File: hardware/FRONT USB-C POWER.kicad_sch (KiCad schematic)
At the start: 40 parts, among them Q3 PMPB11EN,115, Q4 PMPB11EN,115, Q5 PMPB11EN,115, Q6 PMPB11EN,115, U7 LM5143

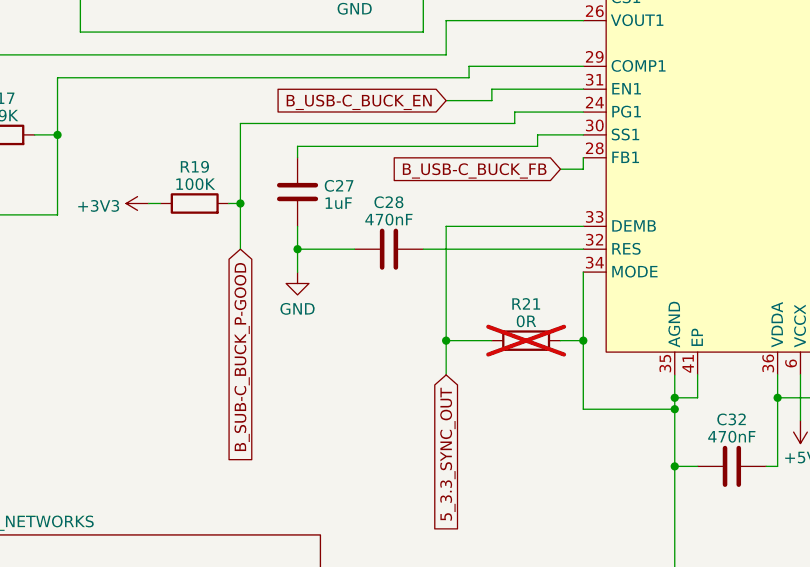
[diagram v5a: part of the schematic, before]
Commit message: switched can tranceiver to combo controler and tranceiver
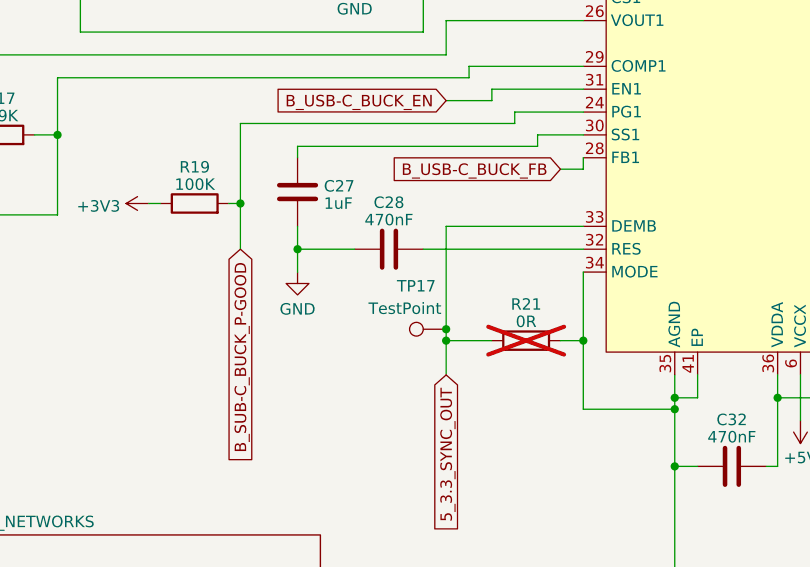
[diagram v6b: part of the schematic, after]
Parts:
- added TP17: TestPoint, TestPoint:TestPoint_Pad_D1.0mm, symbol Connector:TestPoint
- TP10, TP11: footprint TestPoint:TestPoint_Pad_D1.5mm -> TestPoint:TestPoint_Pad_D1.0mm
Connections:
- net 5_3.3_SYNC_OUT: now also TP17.1
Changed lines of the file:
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@@
 	)
 	(junction
+		(at 106.68 128.27)
+		(diameter 0)
+		(color 0 0 0 0)
+	)
+	(junction
 		(at 76.2 72.39)
 		(diameter 0)
@@
 	(wire
 		(pts
-			(xy 106.68 116.84) (xy 106.68 129.54)
+			(xy 106.68 116.84) (xy 106.68 128.27)
+		)
+		(stroke
+			(width 0)
+			(type default)
+		)
+	)
+	(wire
+		(pts
+			(xy 106.68 128.27) (xy 106.68 129.54)
 		)
 		(stroke
@@
 			)
 		)
-		(property "Footprint" "TestPoint:TestPoint_Pad_D1.5mm"
+		(property "Footprint" "TestPoint:TestPoint_Pad_D1.0mm"
 			(at 46.99 72.39 0)
 			(effects
@@
 			)
 		)
-		(property "Footprint" "TestPoint:TestPoint_Pad_D1.5mm"
+		(property "Footprint" "TestPoint:TestPoint_Pad_D1.0mm"
 			(at 238.76 73.66 0)
 			(effects
@@
 					(unit 1)
 				)
+			)
+		)
+	)
+	(symbol
+		(lib_id "Connector:TestPoint")
+		(at 106.68 128.27 90)
+		(unit 1)
+		(exclude_from_sim no)
+		(in_bom yes)
+		(on_board yes)
+		(dnp no)
+		(property "Reference" "TP17"
+			(at 103.378 123.4905 90)
+			(effects
+				(font
+					(size 1.27 1.27)
+				)
+			)
+		)
+		(property "Value" "TestPoint"
+			(at 102.108 125.984 90)
+			(effects
+				(font
+					(size 1.27 1.27)
+				)
+			)
+		)
+		(property "Footprint" "TestPoint:TestPoint_Pad_D1.0mm"
+			(at 106.68 123.19 0)
+			(effects
+				(font
+					(size 1.27 1.27)
+				)
+				(hide yes)
+			)
+		)
+		(property "Datasheet" "~"
+			(at 106.68 123.19 0)
+			(effects
+				(font
+					(size 1.27 1.27)
+				)
+				(hide yes)
+			)
+		)
+		(property "Description" ""
+			(at 106.68 128.27 0)
+			(effects
+				(font
+					(size 1.27 1.27)
+				)
+				(hide yes)
+			)
+		)
+		(pin "1"
+		)
+		(instances
+			(project "usbc-car-module"
+				(path "/fae025e9-99c5-40c1-af6f-99dc1edbfa43/91b561d6-4186-4f6f-8a2c-57c2c305f210"
+					(reference "TP17")
+					(unit 1)
+				)

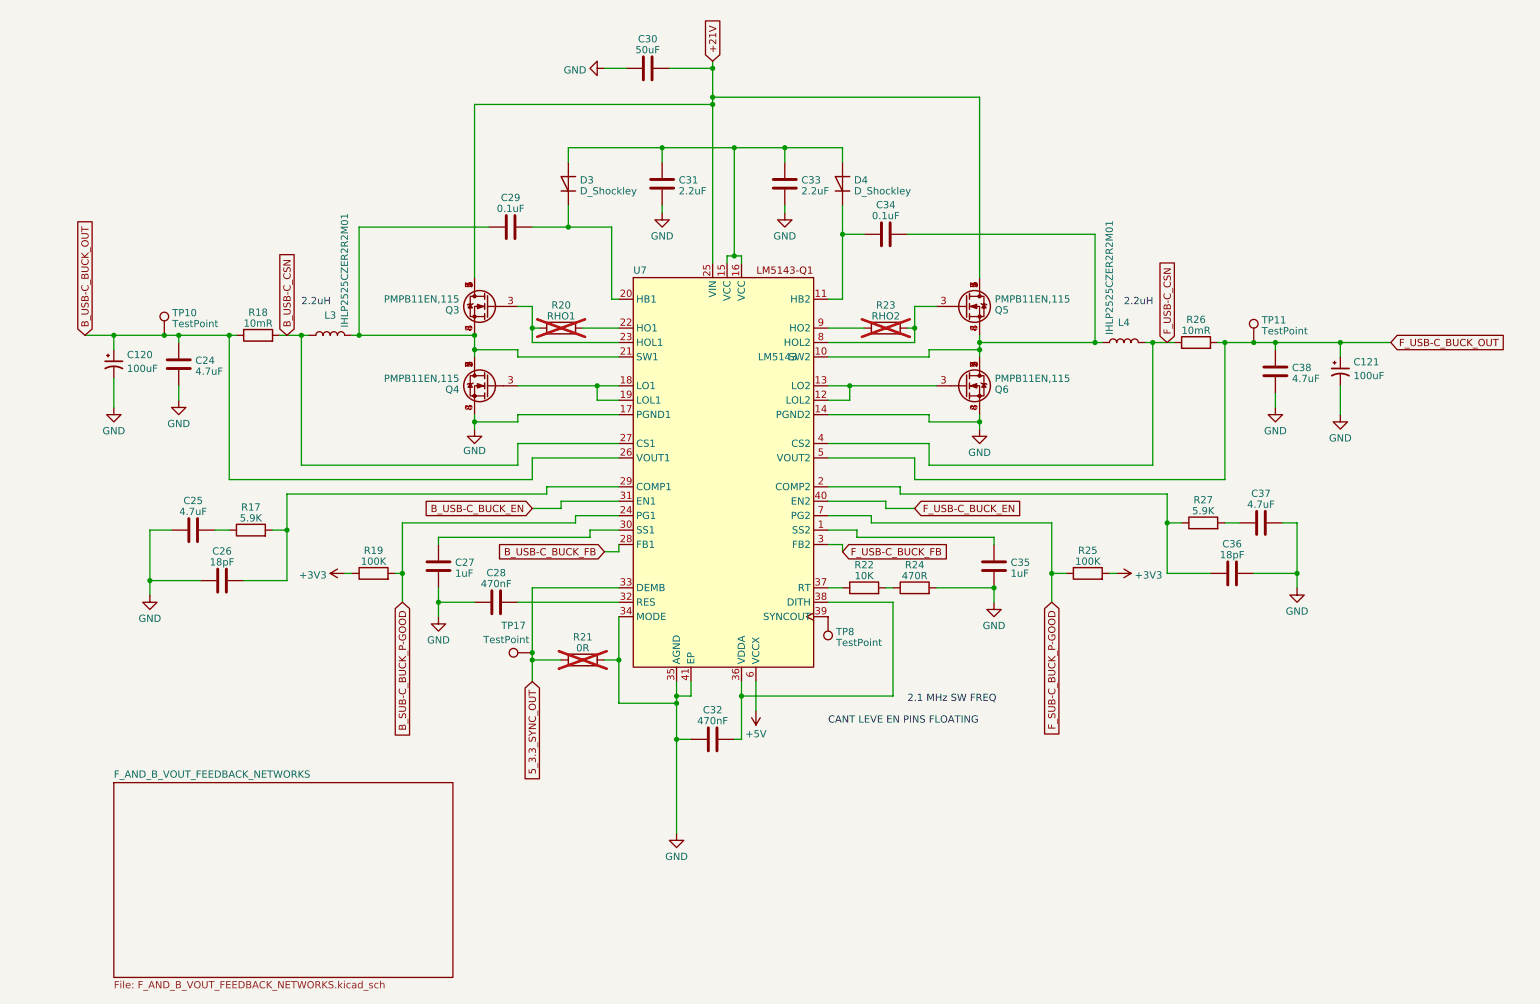
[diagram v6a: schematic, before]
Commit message: migrated to the esp32-s2 and starting new board revison
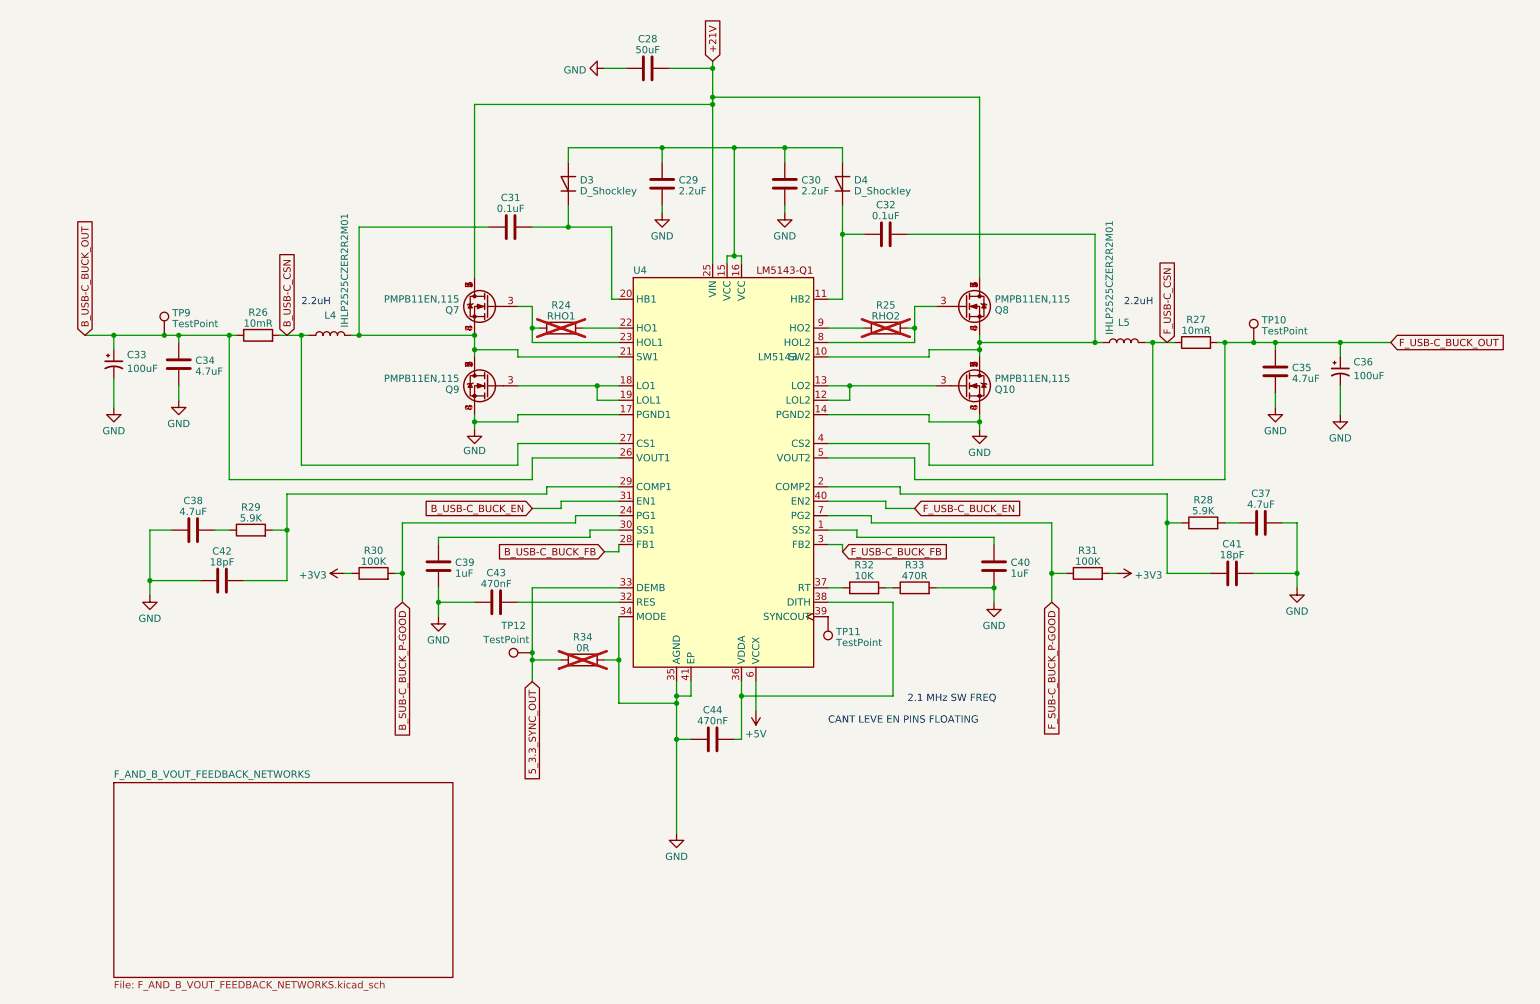
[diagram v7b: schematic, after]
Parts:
- renumbered C30 to C28, C31 to C29, C33 to C30, C29 to C31, C34 to C32, C120 to C33, C24 to C34, C38 to C35, C121 to C36, C25 to C38, C27 to C39, C35 to C40, C36 to C41, C26 to C42, C28 to C43, C32 to C44, L3 to L4, L4 to L5, Q6 to Q10, Q3 to Q7, Q5 to Q8, Q4 to Q9, R20 to R24, R23 to R25, R18 to R26, R26 to R27, R27 to R28, R17 to R29, R19 to R30, R25 to R31, R22 to R32, R24 to R33, R21 to R34, TP11 to TP10, TP8 to TP11, TP17 to TP12, TP10 to TP9, U7 to U4
